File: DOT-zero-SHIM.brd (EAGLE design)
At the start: 30 x 65 mm, 3 parts

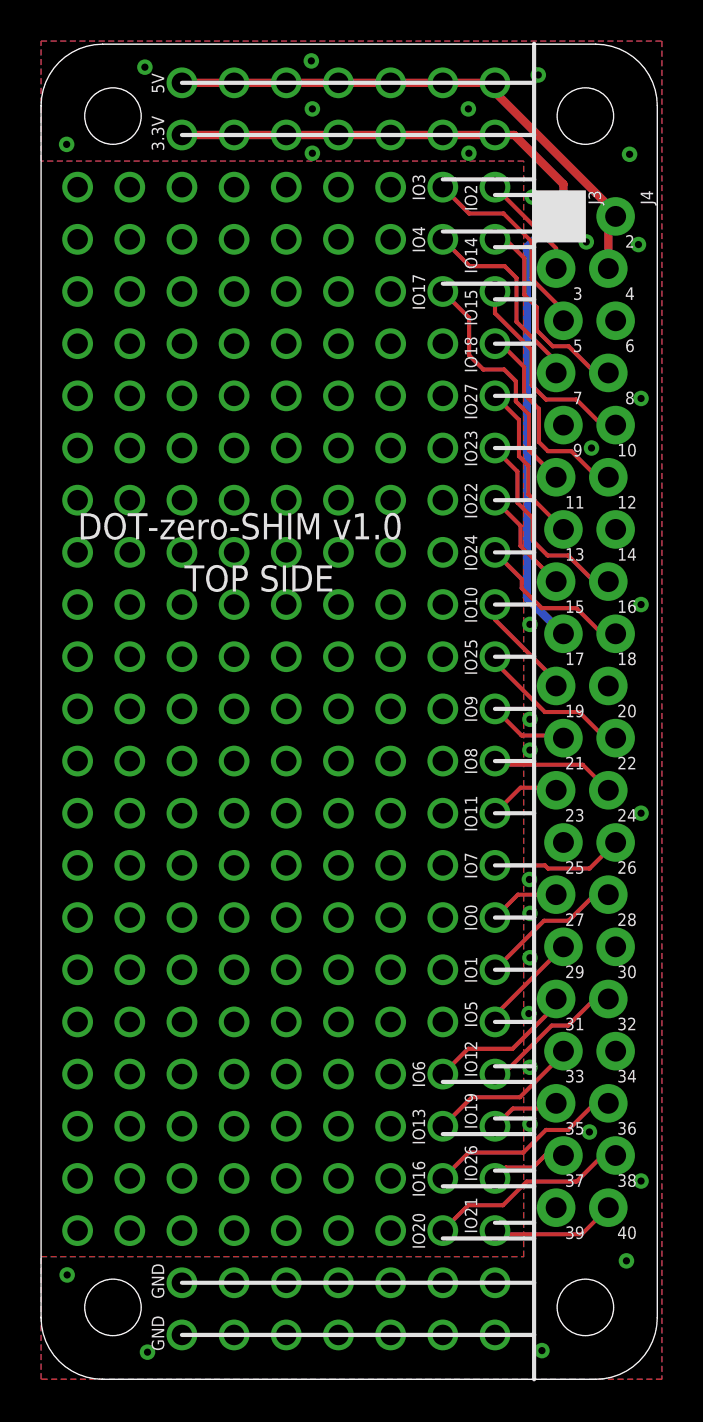
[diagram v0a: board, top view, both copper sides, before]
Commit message: Reworked zero board corners
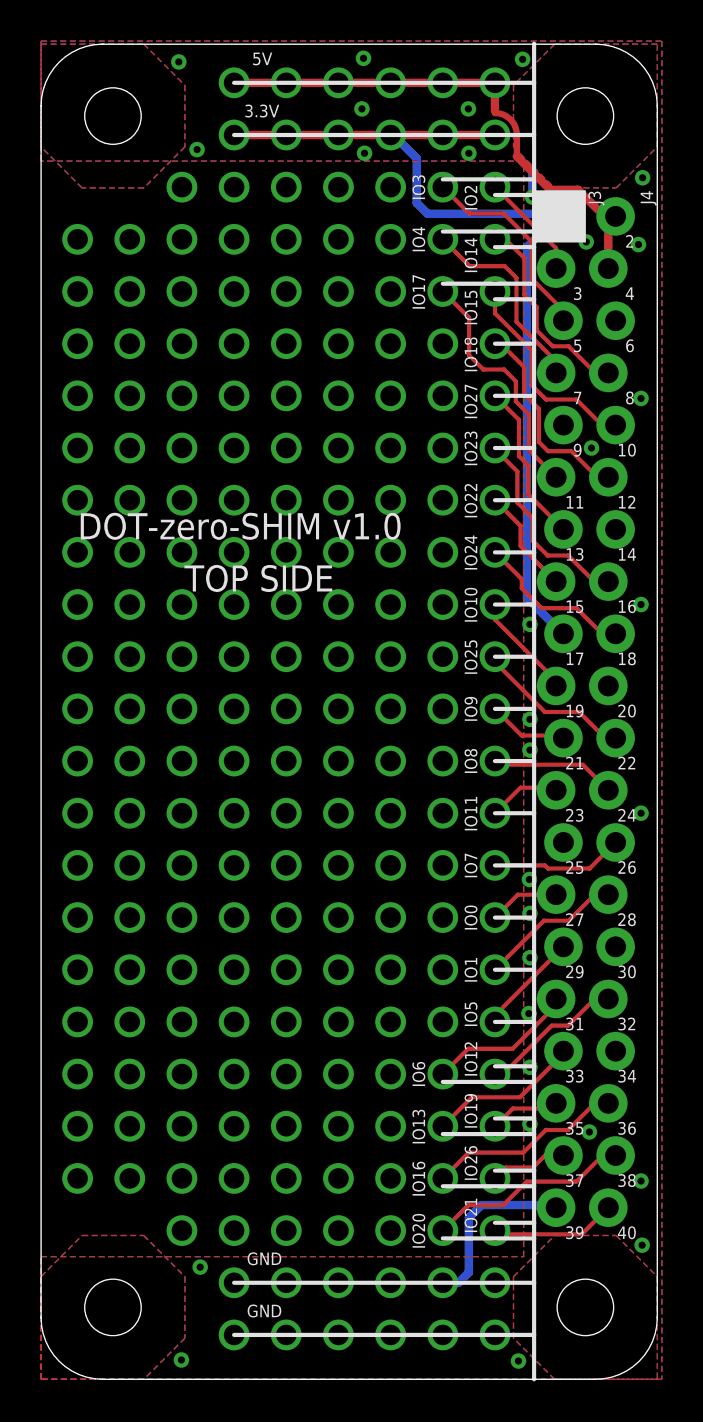
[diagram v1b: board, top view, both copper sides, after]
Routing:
- net GND: track 0.00 -> 11.0 mm, vias 45 -> 43
- net 3.3V: track 43.1 -> 46.0 mm, vias 7 -> 6
- net 5V: track 26.9 -> 25.4 mm, vias 7 -> 6
- added copper zone on layer 1, net GND1
- added copper zone on layer 16, net GND1
